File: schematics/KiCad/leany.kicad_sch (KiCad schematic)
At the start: 29 parts, among them J1 SWD, J2 SSD1306, Q1 DMG6601LVT-7, SW2 ZERO_BTN, SW3 HOLD_BTN, U1 STM32F103C8Tx, U2 AP2112K-3.3, U3 LSM6DSO, Y1 8MHz

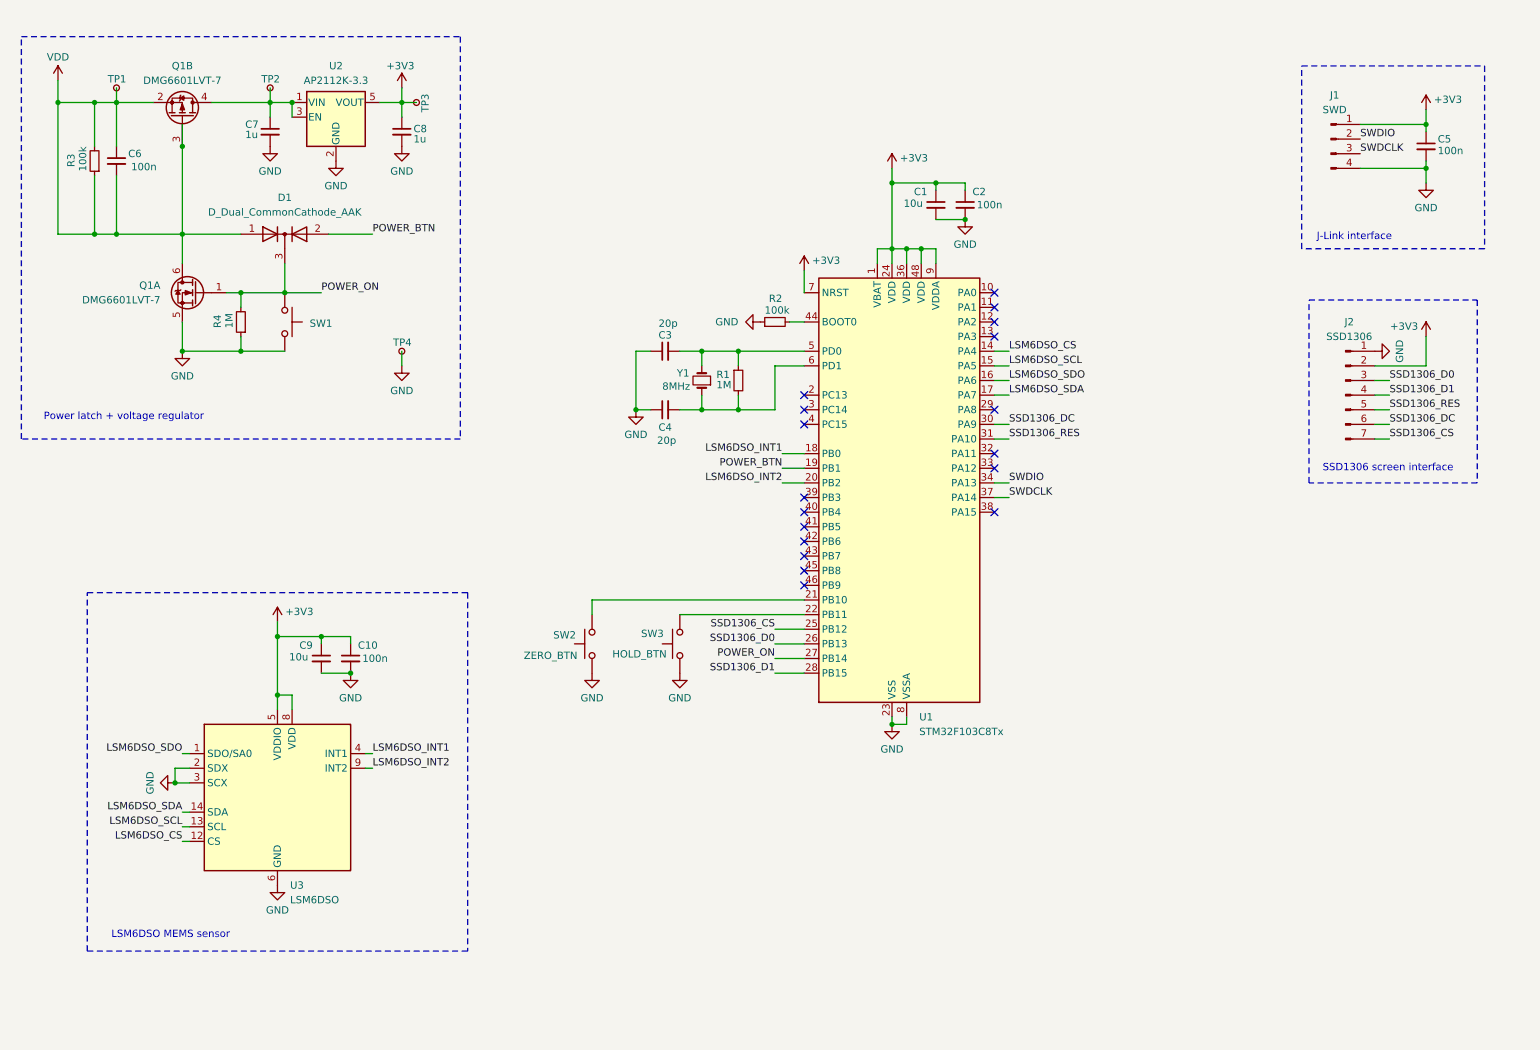
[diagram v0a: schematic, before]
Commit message: add a USB C connector
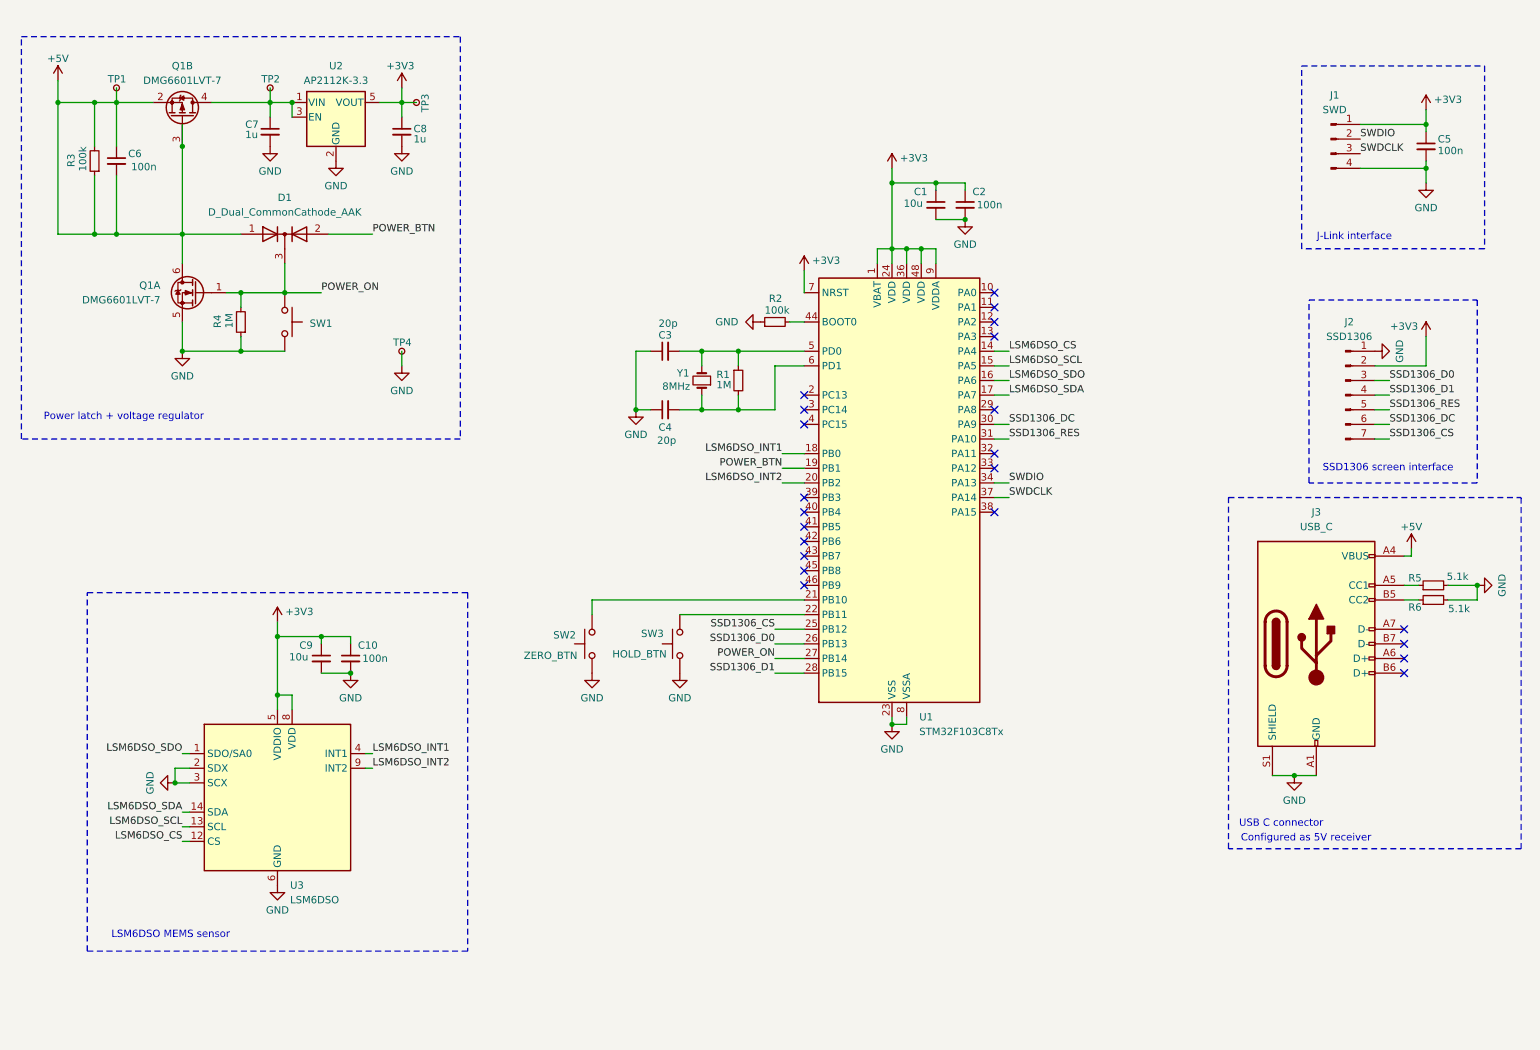
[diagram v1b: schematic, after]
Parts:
- added J3: USB_C, symbol Connector:USB_C_Receptacle_USB2.0_14P
- added R5, R6: 5.1k, Resistor_SMD:R_0603_1608Metric, symbol Device:R_Small
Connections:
- net GND: now also J3.A1 (GND), J3.A12 (GND), J3.B1 (GND), J3.B12 (GND), J3.S1 (SHIELD), R5.2, R6.2
- net VDD renamed +5V
- net +5V: now also J3.A4 (VBUS), J3.A9 (VBUS), J3.B4 (VBUS), J3.B9 (VBUS)
- new net: J3.A5 (CC1), R5.1
- new net: J3.B5 (CC2), R6.1
- no-connect marks 18 -> 22
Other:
- note added: "Configured as 5V receiver"
- note added: "USB C connector"

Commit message: start wiring FTDI chip
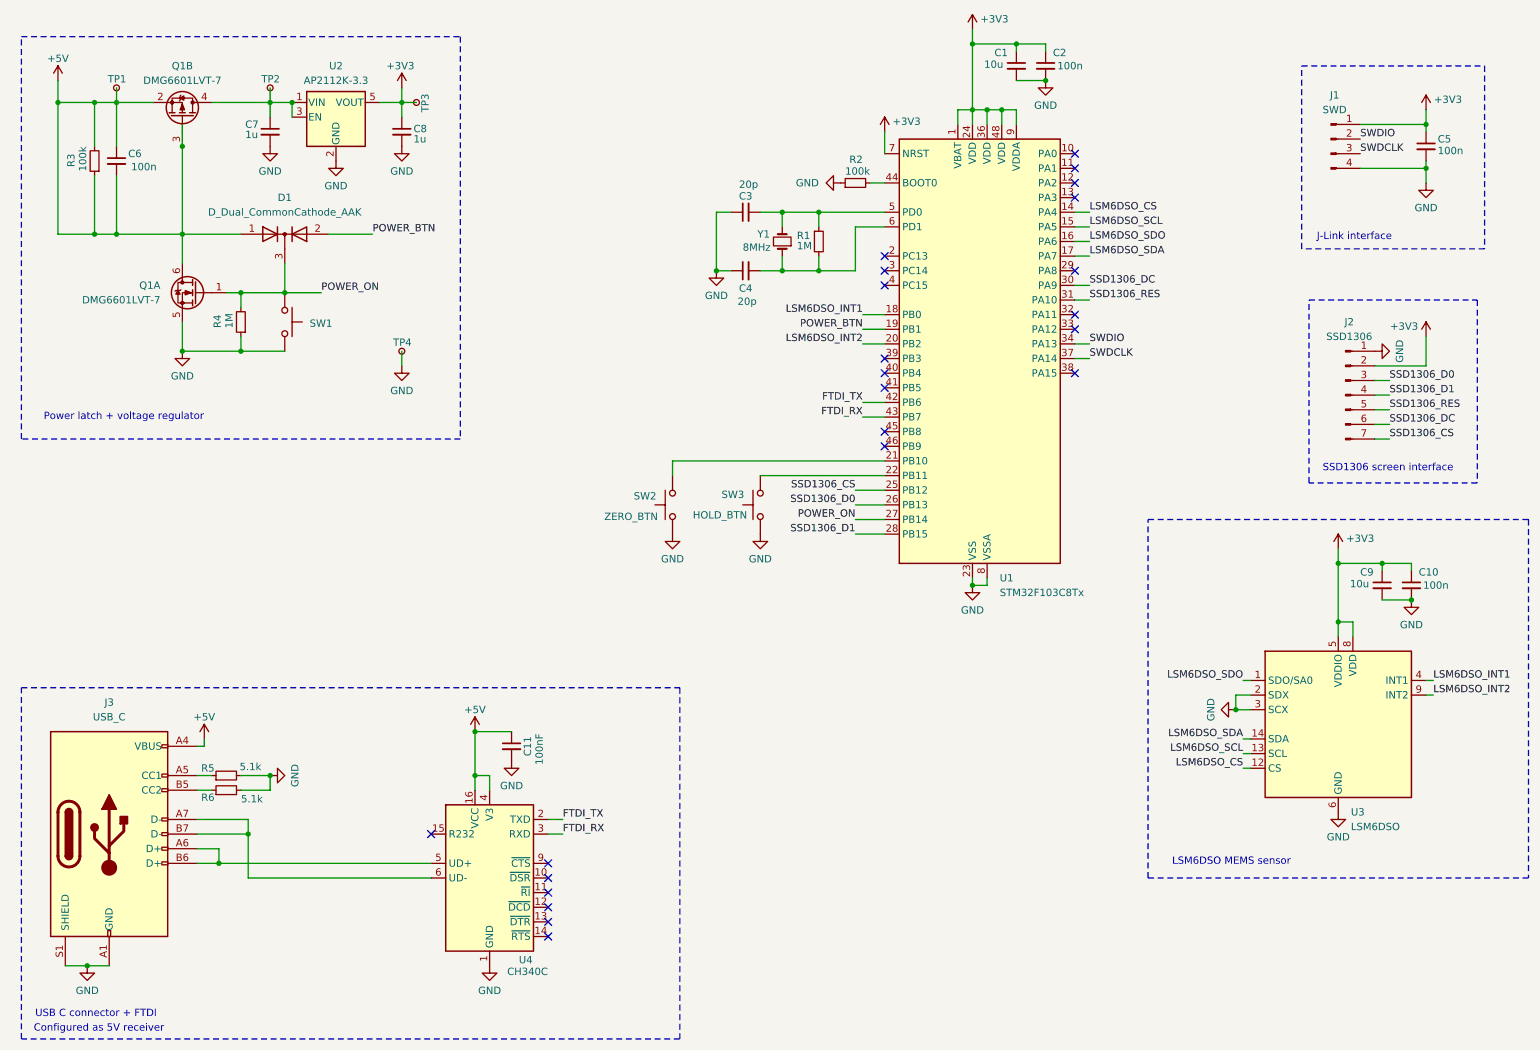
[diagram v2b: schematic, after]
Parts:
- added C11: 100nF, Capacitor_SMD:C_0201_0603Metric, symbol Device:C_Small
- added U4: CH340C, Package_SO:SOIC-16_3.9x9.9mm_P1.27mm, symbol Interface_USB:CH340C
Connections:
- net +5V: now also C11.1, U4.16 (VCC), U4.4 (V3)
- net GND: now also C11.2, U4.1 (GND)
- net FTDI_TX: now reaches U1.42 (PB6)
- net FTDI_TX: now also U4.2 (TXD)
- net FTDI_RX: now reaches U1.43 (PB7)
- net FTDI_RX: now also U4.3 (RXD)
- net at J3.A6 (D+): now also J3.B6 (D+), U4.5 (UD+)
- net at J3.A7 (D-): now also J3.B7 (D-), U4.6 (UD-)
- no-connect marks 22 -> 23
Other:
- note added: "USB C connector + FTDI"
- note removed: "USB C connector"
- moved on the sheet: C1, C10, C2, C3, C4, C9, J3, R1, R2, R5, R6, SW2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

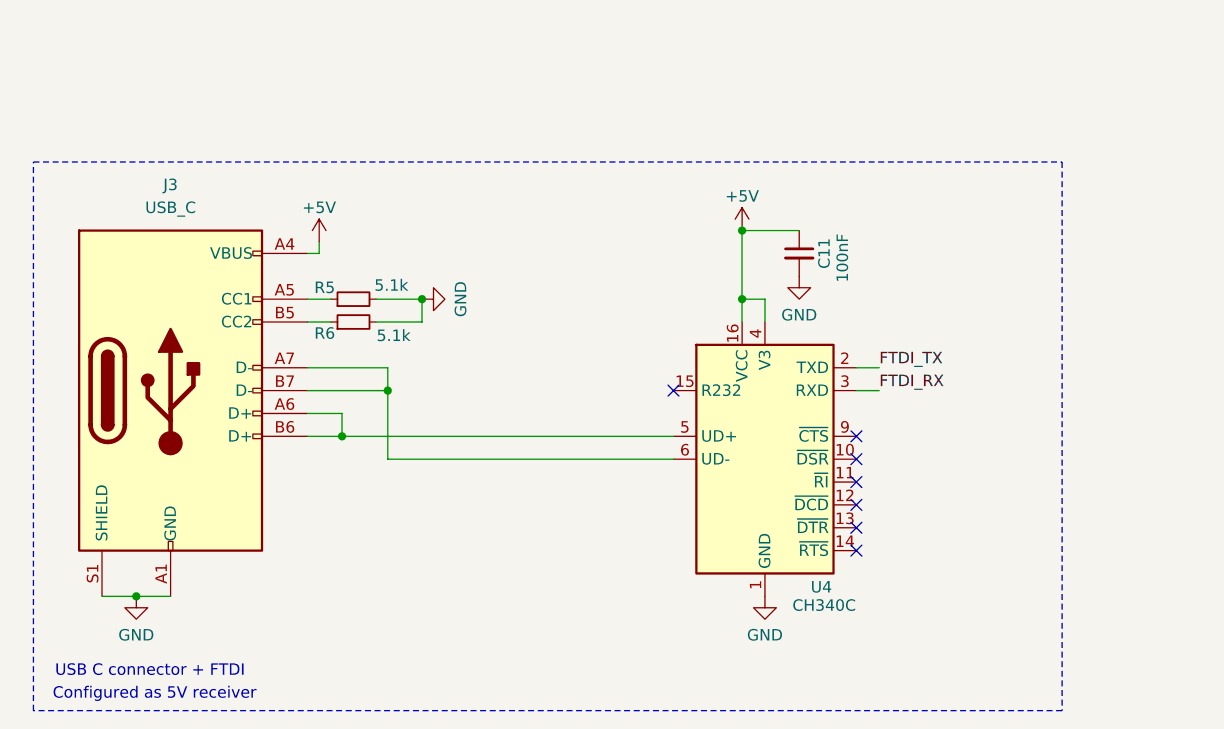
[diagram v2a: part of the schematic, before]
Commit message: reorganise components and add crystal footprint
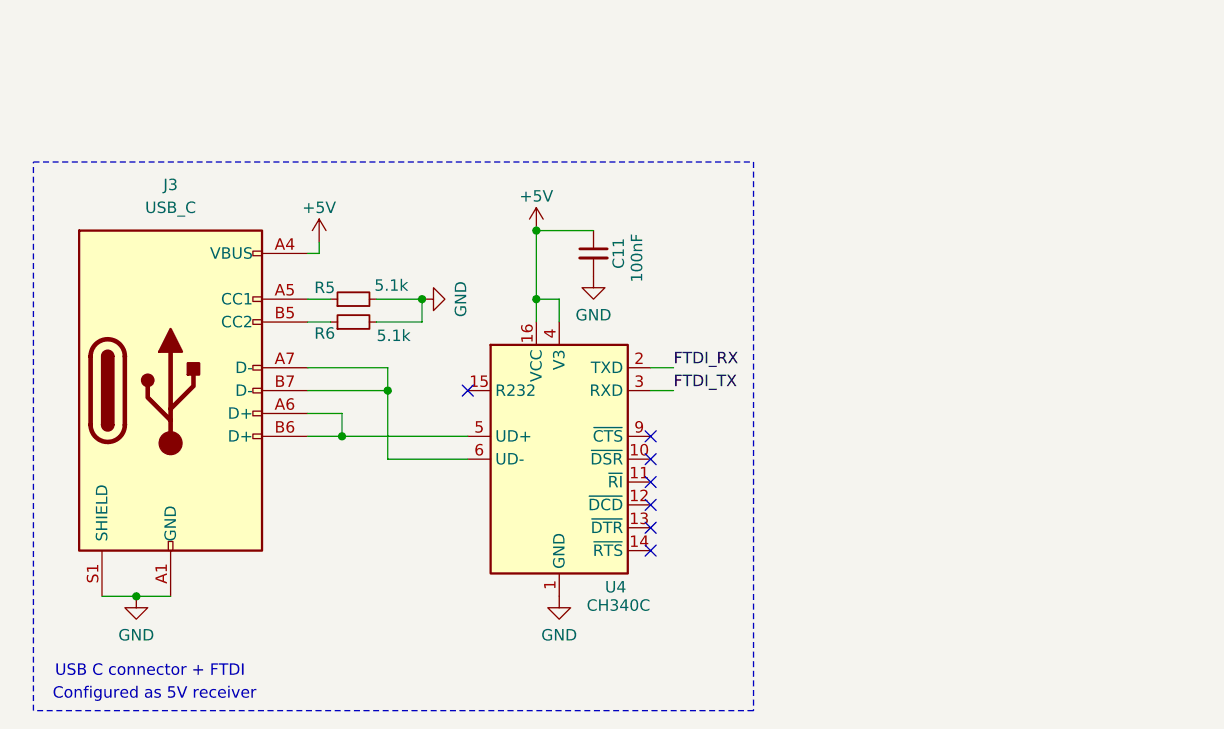
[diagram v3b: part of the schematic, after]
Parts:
- J3: footprint (none) -> Connector_USB:USB_C_Receptacle_GCT_USB4105-xx-A_16P_TopMnt_Horizontal
- Y1: footprint Crystal:Crystal_SMD_0603-2Pin_6.0x3.5mm -> Crystal:Crystal_SMD_Abracon_ABM3-2Pin_5.0x3.2mm
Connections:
- net FTDI_RX: now also U4.2 (TXD); no longer U4.3 (RXD)
- net FTDI_TX: now also U4.3 (RXD); no longer U4.2 (TXD)
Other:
- moved on the sheet: C11, U4
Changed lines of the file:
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@@
 	)
 	(junction
-		(at 96.52 138.43)
+		(at 73.66 138.43)
 		(diameter 0)
 		(color 0 0 0 0)
@@
 	)
 	(junction
-		(at 96.52 146.05)
+		(at 73.66 146.05)
 		(diameter 0)
 		(color 0 0 0 0)
@@
 	)
 	(no_connect
-		(at 109.22 171.45)
+		(at 86.36 171.45)
 	)
 	(no_connect
-		(at 109.22 166.37)
+		(at 86.36 166.37)
 	)
 	(no_connect
@@
 	)
 	(no_connect
-		(at 109.22 173.99)
+		(at 86.36 173.99)
 	)
 	(no_connect
@@
 	)
 	(no_connect
-		(at 109.22 163.83)
+		(at 86.36 163.83)
 	)
 	(no_connect
-		(at 109.22 168.91)
+		(at 86.36 168.91)
 	)
 	(no_connect
-		(at 88.9 156.21)
+		(at 66.04 156.21)
 	)
 	(no_connect
@@
 	)
 	(no_connect
-		(at 109.22 161.29)
+		(at 86.36 161.29)
 	)
 	(wire
@@
 	(wire
 		(pts
-			(xy 88.9 163.83) (xy 57.15 163.83)
+			(xy 66.04 163.83) (xy 57.15 163.83)
 		)
 		(stroke
@@
 	(wire
 		(pts
-			(xy 99.06 146.05) (xy 96.52 146.05)
+			(xy 76.2 146.05) (xy 73.66 146.05)
 		)
 		(stroke
@@
 	(wire
 		(pts
-			(xy 96.52 146.05) (xy 96.52 148.59)
+			(xy 73.66 146.05) (xy 73.66 148.59)
 		)
 		(stroke
@@
 	(wire
 		(pts
-			(xy 96.52 138.43) (xy 102.87 138.43)
+			(xy 73.66 138.43) (xy 80.01 138.43)
 		)
 		(stroke
@@
 	(wire
 		(pts
-			(xy 109.22 153.67) (xy 111.76 153.67)
+			(xy 86.36 153.67) (xy 88.9 153.67)
 		)
 		(stroke
@@
 	(wire
 		(pts
-			(xy 52.07 161.29) (xy 88.9 161.29)
+			(xy 52.07 161.29) (xy 66.04 161.29)
 		)
 		(stroke
@@
 	(wire
 		(pts
-			(xy 99.06 146.05) (xy 99.06 148.59)
+			(xy 76.2 146.05) (xy 76.2 148.59)
 		)
 		(stroke
@@
 	(wire
 		(pts
-			(xy 96.52 138.43) (xy 96.52 146.05)
+			(xy 73.66 138.43) (xy 73.66 146.05)
 		)
 		(stroke
@@
 	(wire
 		(pts
-			(xy 111.76 156.21) (xy 109.22 156.21)
+			(xy 88.9 156.21) (xy 86.36 156.21)
 		)
 		(stroke
@@
 	(rectangle
 		(start 17.78 130.81)
-		(end 132.08 191.77)
+		(end 97.79 191.77)
 		(stroke
 			(width 0)
@@
 	)
 	(label "FTDI_TX"
-		(at 111.76 153.67 0)
+		(at 88.9 156.21 0)
 		(fields_autoplaced yes)
 		(effects
@@
 	)
 	(label "FTDI_RX"
-		(at 111.76 156.21 0)
+		(at 88.9 153.67 0)
 		(fields_autoplaced yes)
 		(effects
@@
 	(symbol
 		(lib_id "power:GND")
-		(at 102.87 143.51 0)
+		(at 80.01 143.51 0)
 		(unit 1)
 		(exclude_from_sim no)
@@
 		(dnp no)
 		(property "Reference" "#PWR029"
-			(at 102.87 149.86 0)
+			(at 80.01 149.86 0)
 			(effects
 				(font
@@
 		)
 		(property "Value" "GND"
-			(at 102.87 147.828 0)
+			(at 80.01 147.828 0)
 			(effects
 				(font
@@
 		)
 		(property "Footprint" ""
-			(at 102.87 143.51 0)
+			(at 80.01 143.51 0)
 			(effects
 				(font
@@
 		)
 		(property "Datasheet" ""
-			(at 102.87 143.51 0)
+			(at 80.01 143.51 0)
 			(effects
 				(font
@@
 		)
 		(property "Description" "Power symbol creates a global label with name \"GND\" , ground"
-			(at 102.87 143.51 0)
+			(at 80.01 143.51 0)
 			(effects
 				(font
@@
 			)
 		)
-		(property "Footprint" ""
+		(property "Footprint" "Connector_USB:USB_C_Receptacle_GCT_USB4105-xx-A_16P_TopMnt_Horizontal"
 			(at 36.83 156.21 0)
 			(effects
@@
 	(symbol
 		(lib_id "Device:C_Small")
-		(at 102.87 140.97 0)
+		(at 80.01 140.97 0)
 		(unit 1)
 		(exclude_from_sim no)
@@
 		(dnp no)
 		(property "Reference" "C11"
-			(at 105.664 140.97 90)
+			(at 82.804 140.97 90)
 			(effects
 				(font
@@
 		)
 		(property "Value" "100nF"
-			(at 107.696 141.478 90)
+			(at 84.836 141.478 90)
 			(effects
 				(font
@@
 		)
 		(property "Footprint" "Capacitor_SMD:C_0201_0603Metric"
-			(at 102.87 140.97 0)
+			(at 80.01 140.97 0)
 			(effects
 				(font
@@
 		)
 		(property "Datasheet" "~"
-			(at 102.87 140.97 0)
+			(at 80.01 140.97 0)
 			(effects
 				(font
@@
 		)
 		(property "Description" "Unpolarized capacitor, small symbol"
-			(at 102.87 140.97 0)
+			(at 80.01 140.97 0)
 			(effects
 				(font
@@
 			)
 		)
-		(property "Footprint" "Crystal:Crystal_SMD_0603-2Pin_6.0x3.5mm"
+		(property "Footprint" "Crystal:Crystal_SMD_Abracon_ABM3-2Pin_5.0x3.2mm"
 			(at 149.86 53.34 0)
 			(effects
@@
 			)
 		)
-		(property "Datasheet" "~"
+		(property "Datasheet" "https://abracon.com/Resonators/ABM3.pdf"
 			(at 149.86 53.34 0)
 			(effects
@@
 	(symbol
 		(lib_id "power:+5V")
-		(at 96.52 138.43 0)
+		(at 73.66 138.43 0)
 		(unit 1)
 		(exclude_from_sim no)
@@
 		(dnp no)
 		(property "Reference" "#PWR027"
-			(at 96.52 142.24 0)
+			(at 73.66 142.24 0)
 			(effects
 				(font
@@
 		)
 		(property "Value" "+5V"
-			(at 96.52 134.62 0)
+			(at 73.66 134.62 0)
 			(effects
 				(font
@@
 		)
 		(property "Footprint" ""
-			(at 96.52 138.43 0)
+			(at 73.66 138.43 0)
 			(effects
 				(font
@@
 		)
 		(property "Datasheet" ""
-			(at 96.52 138.43 0)
+			(at 73.66 138.43 0)
 			(effects
 				(font
@@
 		)
 		(property "Description" "Power symbol creates a global label with name \"+5V\""
-			(at 96.52 138.43 0)
+			(at 73.66 138.43 0)
 			(effects
 				(font
@@
 	(symbol
 		(lib_id "power:GND")
-		(at 99.06 179.07 0)
+		(at 76.2 179.07 0)
 		(unit 1)
 		(exclude_from_sim no)
@@
 		(dnp no)
 		(property "Reference" "#PWR028"
-			(at 99.06 185.42 0)
+			(at 76.2 185.42 0)
 			(effects
 				(font
@@
 		)
 		(property "Value" "GND"
-			(at 99.06 183.388 0)
+			(at 76.2 183.388 0)
 			(effects
 				(font
@@
 		)
 		(property "Footprint" ""
-			(at 99.06 179.07 0)
+			(at 76.2 179.07 0)
 			(effects
 				(font
@@
 		)
 		(property "Datasheet" ""
-			(at 99.06 179.07 0)
+			(at 76.2 179.07 0)
 			(effects
 				(font
@@
 		)
 		(property "Description" "Power symbol creates a global label with name \"GND\" , ground"
-			(at 99.06 179.07 0)
+			(at 76.2 179.07 0)
 			(effects
 				(font
@@
 	(symbol
 		(lib_id "Interface_USB:CH340C")
-		(at 99.06 163.83 0)
+		(at 76.2 163.83 0)
 		(unit 1)
 		(exclude_from_sim no)
@@
 		(dnp no)
 		(property "Reference" "U4"
-			(at 104.14 178.054 0)
+			(at 81.28 178.054 0)
 			(effects
 				(font
@@
 		)
 		(property "Value" "CH340C"
-			(at 102.108 180.086 0)
+			(at 79.248 180.086 0)
 			(effects
 				(font
@@
 		)
 		(property "Footprint" "Package_SO:SOIC-16_3.9x9.9mm_P1.27mm"
-			(at 80.518 133.604 0)
+			(at 57.658 133.604 0)
 			(effects
 				(font
@@
 		)
 		(property "Datasheet" "https://datasheet.lcsc.com/szlcsc/Jiangsu-Qin-Heng-CH340C_C84681.pdf"
-			(at 92.456 130.556 0)
+			(at 69.596 130.556 0)
 			(effects
 				(font
@@
 		)
 		(property "Description" "USB serial converter, crystal-less, UART, SOIC-16"
-			(at 97.536 127.762 0)
+			(at 74.676 127.762 0)
 			(effects
 				(font
